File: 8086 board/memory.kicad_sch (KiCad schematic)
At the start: 42 parts, among them SW34 MEM_BANK, U10 29F800BA, U11 IS61C6416AL, U12 IS61C6416AL, U2 74HC32, U5 74AC573, U6 74AC573, U7 74AC573, U8 74HC138, U9 74HC138

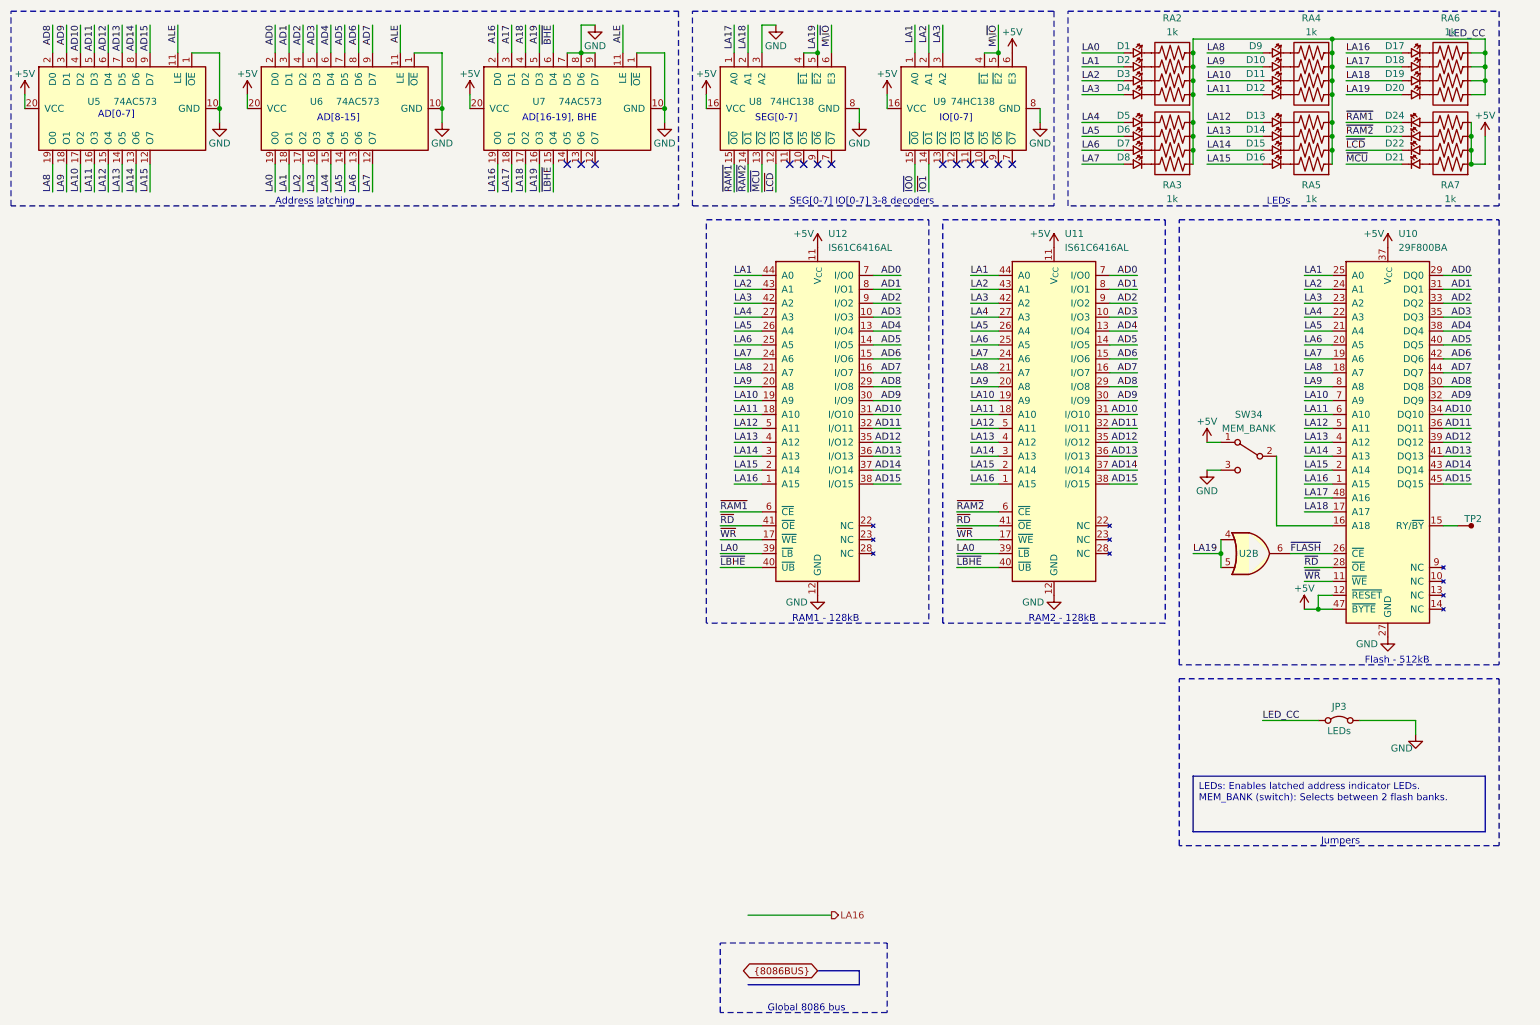
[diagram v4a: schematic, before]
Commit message: schematic: fix LCD RD bug, geographical reannotation
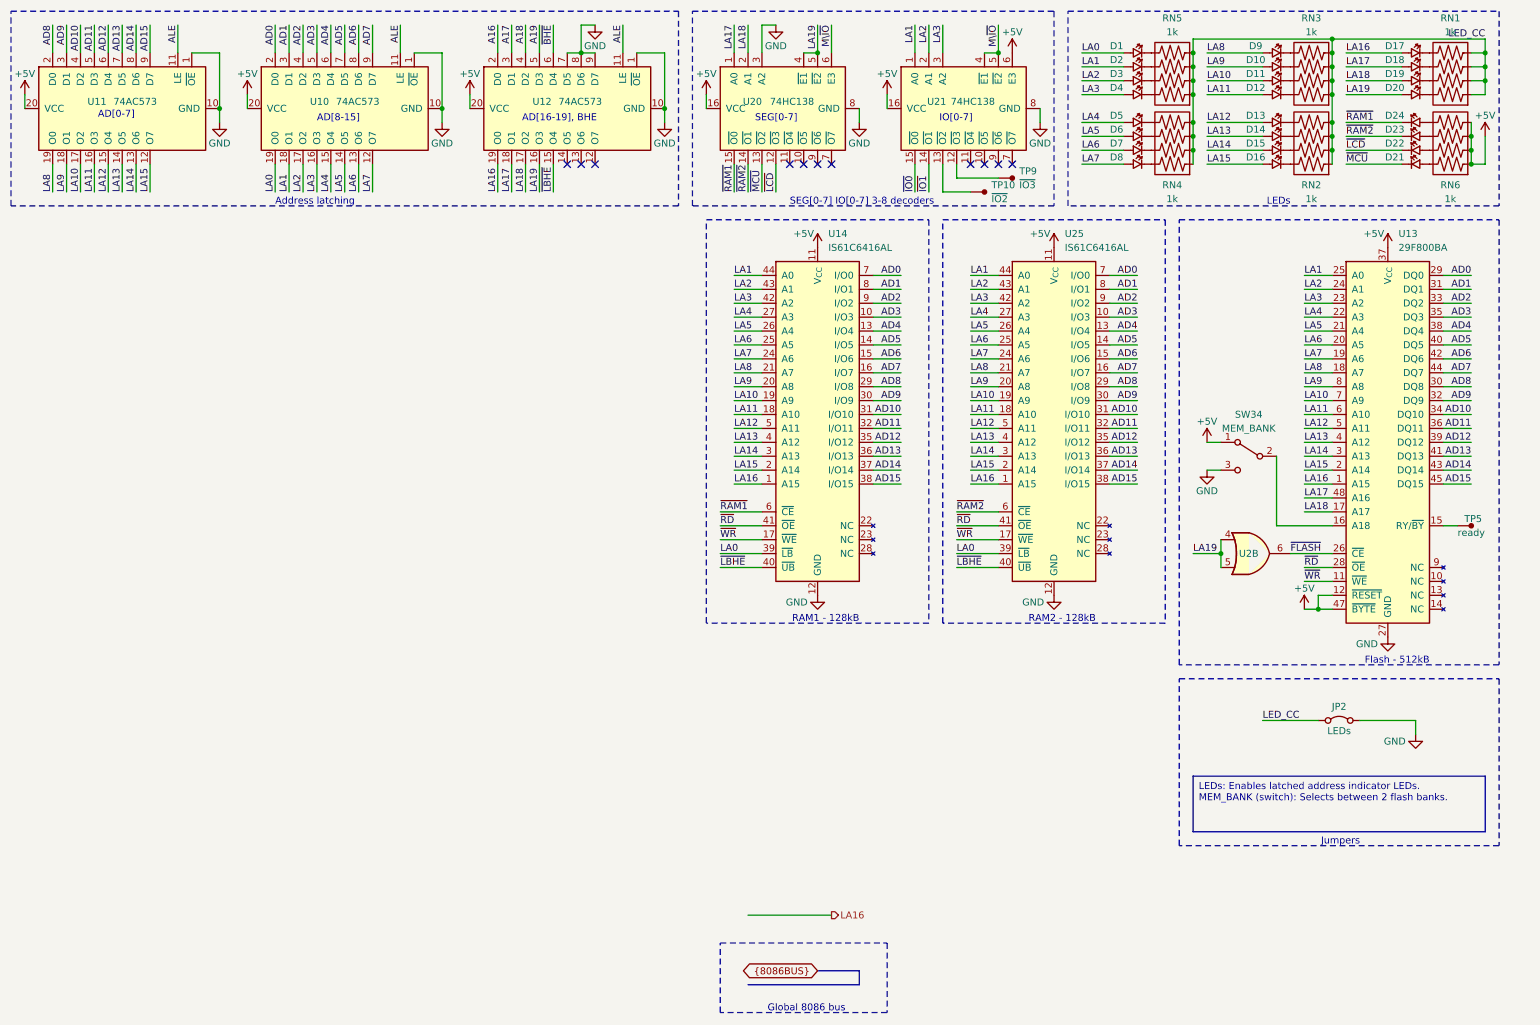
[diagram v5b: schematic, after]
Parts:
- added TP10, TP9: ~, TestPoint:TestPoint_Pad_1.0x1.0mm, symbol 8086PC:TestPoint
- D1: value A0 -> LED; footprint LED_SMD:LED_0603_1608Metric_Pad1.05x0.95mm_HandSolder -> 8086PC:LED_0603_1608Metric_Pad1.05x0.95mm_HandSolder; Indication (none) -> LA0
- D10: value A9 -> LED; footprint LED_SMD:LED_0603_1608Metric_Pad1.05x0.95mm_HandSolder -> 8086PC:LED_0603_1608Metric_Pad1.05x0.95mm_HandSolder; Indication (none) -> LA9
- D11: value A10 -> LED; footprint LED_SMD:LED_0603_1608Metric_Pad1.05x0.95mm_HandSolder -> 8086PC:LED_0603_1608Metric_Pad1.05x0.95mm_HandSolder; Indication (none) -> LA10
- D12: value A11 -> LED; footprint LED_SMD:LED_0603_1608Metric_Pad1.05x0.95mm_HandSolder -> 8086PC:LED_0603_1608Metric_Pad1.05x0.95mm_HandSolder; Indication (none) -> LA11
- D13: value A12 -> LED; footprint LED_SMD:LED_0603_1608Metric_Pad1.05x0.95mm_HandSolder -> 8086PC:LED_0603_1608Metric_Pad1.05x0.95mm_HandSolder; Indication (none) -> LA12
- D14: value A13 -> LED; footprint LED_SMD:LED_0603_1608Metric_Pad1.05x0.95mm_HandSolder -> 8086PC:LED_0603_1608Metric_Pad1.05x0.95mm_HandSolder; Indication (none) -> LA13
- D15: value A14 -> LED; footprint LED_SMD:LED_0603_1608Metric_Pad1.05x0.95mm_HandSolder -> 8086PC:LED_0603_1608Metric_Pad1.05x0.95mm_HandSolder; Indication (none) -> LA14
- D16: value A15 -> LED; footprint LED_SMD:LED_0603_1608Metric_Pad1.05x0.95mm_HandSolder -> 8086PC:LED_0603_1608Metric_Pad1.05x0.95mm_HandSolder; Indication (none) -> LA15
- D17: value A16 -> LED; footprint LED_SMD:LED_0603_1608Metric_Pad1.05x0.95mm_HandSolder -> 8086PC:LED_0603_1608Metric_Pad1.05x0.95mm_HandSolder; Indication (none) -> LA16
- D18: value A17 -> LED; footprint LED_SMD:LED_0603_1608Metric_Pad1.05x0.95mm_HandSolder -> 8086PC:LED_0603_1608Metric_Pad1.05x0.95mm_HandSolder; Indication (none) -> LA17
- D19: value A18 -> LED; footprint LED_SMD:LED_0603_1608Metric_Pad1.05x0.95mm_HandSolder -> 8086PC:LED_0603_1608Metric_Pad1.05x0.95mm_HandSolder; Indication (none) -> LA18
- D2: value A1 -> LED; footprint LED_SMD:LED_0603_1608Metric_Pad1.05x0.95mm_HandSolder -> 8086PC:LED_0603_1608Metric_Pad1.05x0.95mm_HandSolder; Indication (none) -> LA1
- D20: value A19 -> LED; footprint LED_SMD:LED_0603_1608Metric_Pad1.05x0.95mm_HandSolder -> 8086PC:LED_0603_1608Metric_Pad1.05x0.95mm_HandSolder; Indication (none) -> LA19
- D21: value MCU -> LED; footprint LED_SMD:LED_0603_1608Metric_Pad1.05x0.95mm_HandSolder -> 8086PC:LED_0603_1608Metric_Pad1.05x0.95mm_HandSolder; Indication (none) -> MCU
- D22: value LCD -> LED; footprint LED_SMD:LED_0603_1608Metric_Pad1.05x0.95mm_HandSolder -> 8086PC:LED_0603_1608Metric_Pad1.05x0.95mm_HandSolder; Indication (none) -> LCD
- D23: value RAM2 -> LED; footprint LED_SMD:LED_0603_1608Metric_Pad1.05x0.95mm_HandSolder -> 8086PC:LED_0603_1608Metric_Pad1.05x0.95mm_HandSolder; Indication (none) -> RAM2
- D24: value RAM1 -> LED; footprint LED_SMD:LED_0603_1608Metric_Pad1.05x0.95mm_HandSolder -> 8086PC:LED_0603_1608Metric_Pad1.05x0.95mm_HandSolder; Indication (none) -> RAM1
- D3: value A2 -> LED; footprint LED_SMD:LED_0603_1608Metric_Pad1.05x0.95mm_HandSolder -> 8086PC:LED_0603_1608Metric_Pad1.05x0.95mm_HandSolder; Indication (none) -> LA2
- D4: value A3 -> LED; footprint LED_SMD:LED_0603_1608Metric_Pad1.05x0.95mm_HandSolder -> 8086PC:LED_0603_1608Metric_Pad1.05x0.95mm_HandSolder; Indication (none) -> LA3
- D5: value A4 -> LED; footprint LED_SMD:LED_0603_1608Metric_Pad1.05x0.95mm_HandSolder -> 8086PC:LED_0603_1608Metric_Pad1.05x0.95mm_HandSolder; Indication (none) -> LA4
- D6: value A5 -> LED; footprint LED_SMD:LED_0603_1608Metric_Pad1.05x0.95mm_HandSolder -> 8086PC:LED_0603_1608Metric_Pad1.05x0.95mm_HandSolder; Indication (none) -> LA5
- D7: value A6 -> LED; footprint LED_SMD:LED_0603_1608Metric_Pad1.05x0.95mm_HandSolder -> 8086PC:LED_0603_1608Metric_Pad1.05x0.95mm_HandSolder; Indication (none) -> LA6
- D8: value A7 -> LED; footprint LED_SMD:LED_0603_1608Metric_Pad1.05x0.95mm_HandSolder -> 8086PC:LED_0603_1608Metric_Pad1.05x0.95mm_HandSolder; Indication (none) -> LA7
- D9: value A8 -> LED; footprint LED_SMD:LED_0603_1608Metric_Pad1.05x0.95mm_HandSolder -> 8086PC:LED_0603_1608Metric_Pad1.05x0.95mm_HandSolder; Indication (none) -> LA8
- JP2: renamed from JP3; now left out of the parts list
- SW34: value MEM_BANK -> ~; Key (none) -> MEM_BANK
- TP5: renamed from TP2; Signal (none) -> ready; now left out of the parts list
- U2: now in the parts list
- renumbered RA6 to RN1, RA5 to RN2, RA4 to RN3, RA3 to RN4, RA2 to RN5, RA7 to RN6, U6 to U10, U5 to U11, U7 to U12, U10 to U13, U12 to U14, U8 to U20, U9 to U21, U11 to U25
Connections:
- net at U21.12 (~{O3}): now also TP9.1
- net at U21.13 (~{O2}): now also TP10.1
- no-connect marks 13 -> 11
